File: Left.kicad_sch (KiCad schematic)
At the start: 30 parts, among them J5 Conn_01x02, U1 LM1117-3.3, U10 RP2040, U8 W25Q128JVS, Y2 ECS-120-8-33-JGN-TR3

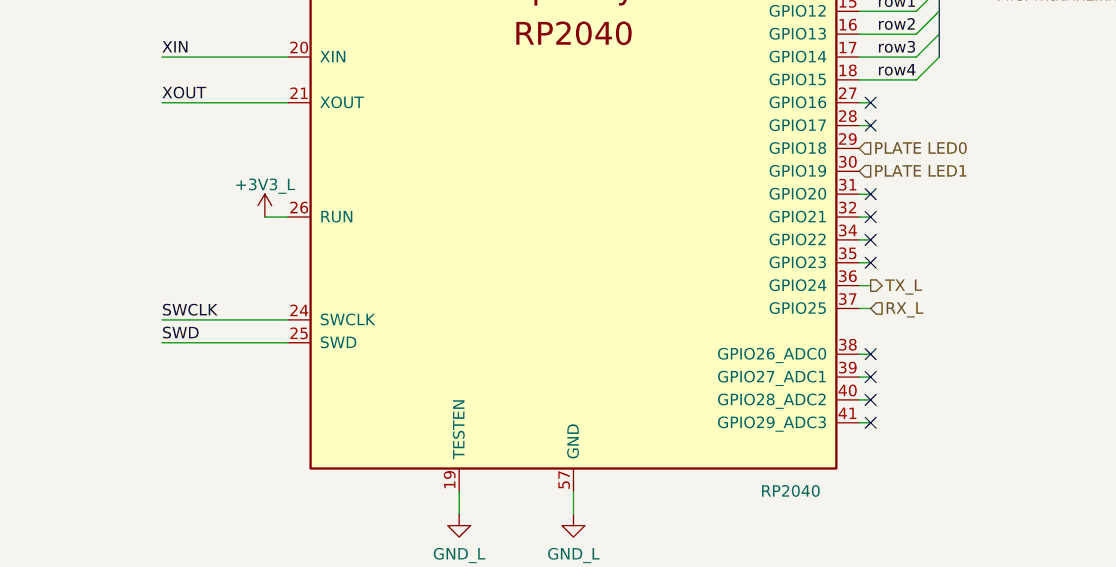
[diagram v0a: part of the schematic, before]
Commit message: Left side case created in blender
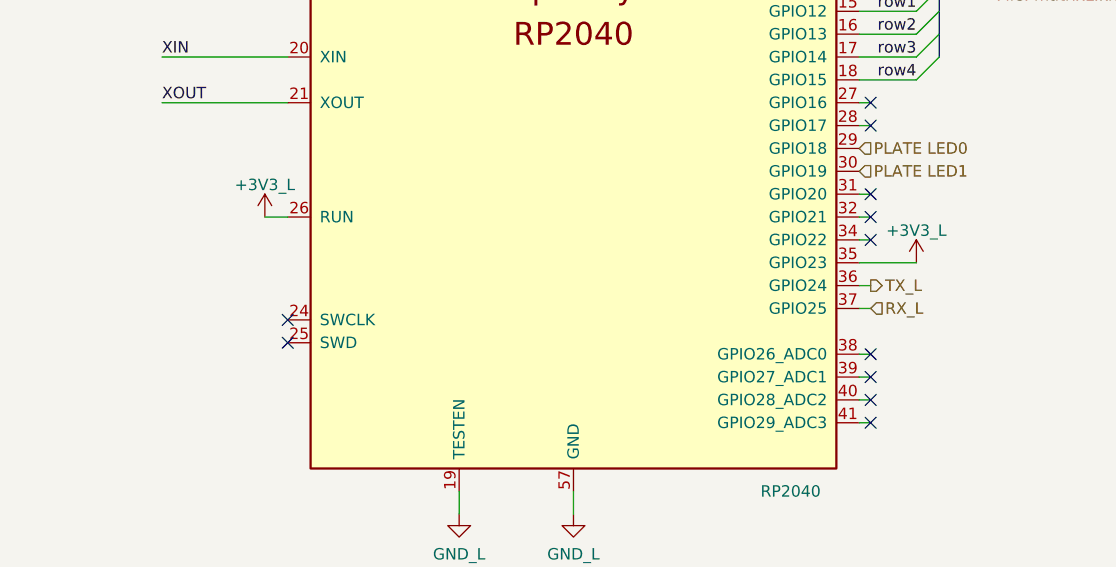
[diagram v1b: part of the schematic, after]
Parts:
- H1, H3, H4: footprint MountingHole:MountingHole_3.2mm_M3_Pad_Via -> arisu-split:aluminium profile nut
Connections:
- net +3V3_L: now also U10.35 (GPIO23)
- net SWCLK: no longer names the net of U10.24 (SWCLK)
- net SWD: no longer names the net of U10.25 (SWD)
- no-connect marks 14 -> 15
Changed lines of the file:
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@@
   (no_connect (at 200.66 78.74))
   (no_connect (at 201.93 149.86))
-  (no_connect (at 201.93 137.16))
+  (no_connect (at 137.16 143.51))
   (no_connect (at 201.93 129.54))
   (no_connect (at 200.66 83.82))
@@
   (no_connect (at 200.66 81.28))
   (no_connect (at 201.93 152.4))
+  (no_connect (at 137.16 146.05))
   (bus_entry (at 209.55 88.9) (size -2.54 2.54)
     (stroke (width 0) (type default) (color 0 0 0 0))
@@
     (stroke (width 0) (type default) (color 0 0 0 0))
   )
-  (wire (pts (xy 137.16 146.05) (xy 123.19 146.05))
-    (stroke (width 0) (type default) (color 0 0 0 0))
-  )
   (wire (pts (xy 123.19 91.44) (xy 137.16 91.44))
     (stroke (width 0) (type default) (color 0 0 0 0))
@@
     (stroke (width 0) (type default) (color 0 0 0 0))
   )
-  (wire (pts (xy 137.16 143.51) (xy 123.19 143.51))
-    (stroke (width 0) (type default) (color 0 0 0 0))
-  )
   (wire (pts (xy 45.72 163.83) (xy 59.69 163.83))
     (stroke (width 0) (type default) (color 0 0 0 0))
@@
     (stroke (width 0) (type default) (color 0 0 0 0))
   )
-  (wire (pts (xy 201.93 137.16) (xy 200.66 137.16))
+  (wire (pts (xy 200.66 137.16) (xy 207.01 137.16))
     (stroke (width 0) (type default) (color 0 0 0 0))
   )
@@
     (effects (font (size 1.27 1.27)) (justify right bottom))
   )
-  (label "SWD" (at 123.19 146.05 0)
-    (effects (font (size 1.27 1.27)) (justify left bottom))
-  )
   (label "1V1" (at 148.59 27.94 180)
     (effects (font (size 1.27 1.27)) (justify right bottom))
@@
     (effects (font (size 1.27 1.27)) (justify right bottom))
   )
-  (label "SWCLK" (at 123.19 143.51 0)
-    (effects (font (size 1.27 1.27)) (justify left bottom))
-  )
   (label "col3" (at 207.01 93.98 180)
     (effects (font (size 1.27 1.27)) (justify right bottom))
@@
       (effects (font (size 1.27 1.27)) (justify left))
     )
-    (property "Footprint" "MountingHole:MountingHole_3.2mm_M3_Pad_Via" (id 2) (at 154.94 187.96 0)
+    (property "Footprint" "arisu-split:aluminium profile nut" (id 2) (at 154.94 187.96 0)
       (effects (font (size 1.27 1.27)) hide)
     )
@@
       (effects (font (size 1.27 1.27)) (justify left))
     )
-    (property "Footprint" "MountingHole:MountingHole_3.2mm_M3_Pad_Via" (id 2) (at 132.08 187.96 0)
+    (property "Footprint" "arisu-split:aluminium profile nut" (id 2) (at 132.08 187.96 0)
       (effects (font (size 1.27 1.27)) hide)
     )
@@
       (effects (font (size 1.27 1.27)) (justify left))
     )
-    (property "Footprint" "MountingHole:MountingHole_3.2mm_M3_Pad_Via" (id 2) (at 132.08 175.26 0)
+    (property "Footprint" "arisu-split:aluminium profile nut" (id 2) (at 132.08 175.26 0)
       (effects (font (size 1.27 1.27)) hide)
     )
@@
     (pin "2")
   )
+  (symbol (lib_id "arisu-split:+3V3_L") (at 207.01 137.16 0) (unit 1)
+    (in_bom yes) (on_board yes) (fields_autoplaced)
+    (property "Reference" "#PWR0165" (id 0) (at 207.01 140.97 0)
+      (effects (font (size 1.27 1.27)) hide)
+    )
+    (property "Value" "+3V3_L" (id 1) (at 207.01 133.5842 0))
+    (property "Footprint" "" (id 2) (at 207.01 137.16 0)
+      (effects (font (size 1.27 1.27)) hide)
+    )
+    (property "Datasheet" "" (id 3) (at 207.01 137.16 0)
+      (effects (font (size 1.27 1.27)) hide)
+    )
+    (pin "1")
+  )
   (symbol (lib_id "Device:R") (at 215.9 63.5 270) (unit 1)

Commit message: replace usb right side, rotate micro, add protection diodes, trrs protection circuit mirrored, run pin cap removved, resistor footprints replaced
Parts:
- R13, R14, R16, R17: footprint Capacitor_SMD:C_0603_1608Metric -> Resistor_SMD:R_0603_1608Metric
- R15: footprint Capacitor_SMD:C_0402_1005Metric -> Resistor_SMD:R_0402_1005Metric
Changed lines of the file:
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@@
     (property "Reference" "R15" (id 0) (at 63.5 158.5722 90))
     (property "Value" "1k" (id 1) (at 63.5 160.8836 90))
-    (property "Footprint" "Capacitor_SMD:C_0402_1005Metric" (id 2) (at 63.5 162.052 90)
+    (property "Footprint" "Resistor_SMD:R_0402_1005Metric" (id 2) (at 63.5 162.052 90)
       (effects (font (size 1.27 1.27)) hide)
     )
@@
     (property "Reference" "R17" (id 0) (at 215.9 65.8622 90))
     (property "Value" "27" (id 1) (at 215.9 68.1736 90))
-    (property "Footprint" "Capacitor_SMD:C_0603_1608Metric" (id 2) (at 215.9 69.342 90)
+    (property "Footprint" "Resistor_SMD:R_0603_1608Metric" (id 2) (at 215.9 69.342 90)
       (effects (font (size 1.27 1.27)) hide)
     )
@@
       (effects (font (size 1.27 1.27)) (justify left))
     )
-    (property "Footprint" "Capacitor_SMD:C_0603_1608Metric" (id 2) (at 56.642 86.36 90)
+    (property "Footprint" "Resistor_SMD:R_0603_1608Metric" (id 2) (at 56.642 86.36 90)
       (effects (font (size 1.27 1.27)) hide)
     )
@@
     (property "Reference" "R13" (id 0) (at 43.18 96.3422 90))
     (property "Value" "1k" (id 1) (at 43.18 98.6536 90))
-    (property "Footprint" "Capacitor_SMD:C_0603_1608Metric" (id 2) (at 43.18 99.822 90)
+    (property "Footprint" "Resistor_SMD:R_0603_1608Metric" (id 2) (at 43.18 99.822 90)
       (effects (font (size 1.27 1.27)) hide)
     )
@@
     (property "Reference" "R16" (id 0) (at 215.9 58.2422 90))
     (property "Value" "27" (id 1) (at 215.9 60.5536 90))
-    (property "Footprint" "Capacitor_SMD:C_0603_1608Metric" (id 2) (at 215.9 61.722 90)
-      (effects (font (size 1.27 1.27)) hide)
-    )
+    (property "Footprint" "Resistor_SMD:R_0603_1608Metric" (id 2) (at 215.9 61.722 90)
+      (effects (font (size 1.27 1.27)) hide)
+    )

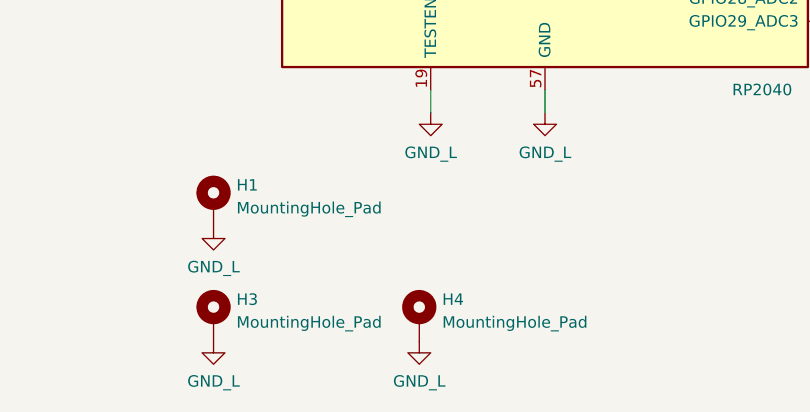
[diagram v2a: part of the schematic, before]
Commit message: Add back logo, improve layers for 3d model, remove silkscreen designators, basically fix right pcb
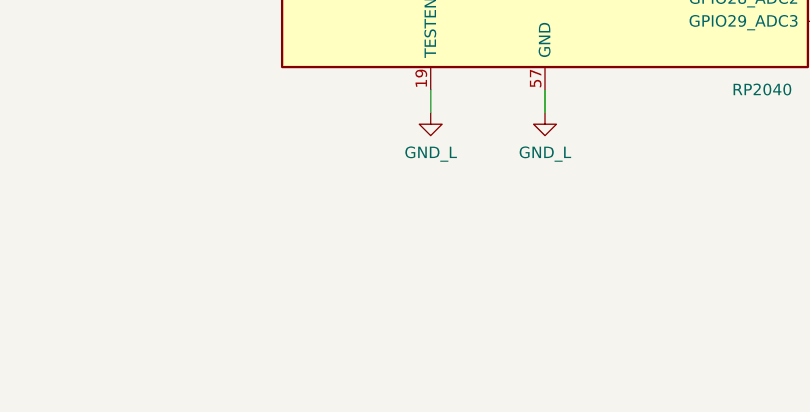
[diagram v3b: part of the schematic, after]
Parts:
- removed H1, H3, H4: MountingHole_Pad, arisu-split:aluminium profile nut, symbol Mechanical:MountingHole_Pad
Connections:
- net PLATE  LED1 renamed PLATE LED1
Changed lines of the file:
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@@
     (effects (font (size 1.27 1.27)) (justify left))
   )
-  (hierarchical_label "PLATE  LED1" (shape input) (at 200.66 127 0)
+  (hierarchical_label "PLATE LED1" (shape input) (at 200.66 127 0)
     (effects (font (size 1.27 1.27)) (justify left))
   )
@@
     (pin "1")
     (pin "2")
-  )
-  (symbol (lib_id "Mechanical:MountingHole_Pad") (at 154.94 187.96 0) (unit 1)
-    (in_bom yes) (on_board yes) (fields_autoplaced)
-    (property "Reference" "H4" (id 0) (at 157.48 185.8553 0)
-      (effects (font (size 1.27 1.27)) (justify left))
-    )
-    (property "Value" "MountingHole_Pad" (id 1) (at 157.48 188.3922 0)
-      (effects (font (size 1.27 1.27)) (justify left))
-    )
-    (property "Footprint" "arisu-split:aluminium profile nut" (id 2) (at 154.94 187.96 0)
-      (effects (font (size 1.27 1.27)) hide)
-    )
-    (property "Datasheet" "~" (id 3) (at 154.94 187.96 0)
-      (effects (font (size 1.27 1.27)) hide)
-    )
-    (pin "1")
   )
   (symbol (lib_id "Device:R") (at 63.5 163.83 270) (unit 1)
@@
     (pin "2")
   )
-  (symbol (lib_id "arisu-split:GND_L") (at 132.08 177.8 0) (unit 1)
-    (in_bom yes) (on_board yes) (fields_autoplaced)
-    (property "Reference" "#PWR0153" (id 0) (at 132.08 184.15 0)
-      (effects (font (size 1.27 1.27)) hide)
-    )
-    (property "Value" "GND_L" (id 1) (at 132.08 182.2434 0))
-    (property "Footprint" "" (id 2) (at 132.08 177.8 0)
-      (effects (font (size 1.27 1.27)) hide)
-    )
-    (property "Datasheet" "" (id 3) (at 132.08 177.8 0)
-      (effects (font (size 1.27 1.27)) hide)
-    )
-    (pin "1")
-  )
   (symbol (lib_id "arisu-split:GND_L") (at 128.27 39.37 0) (unit 1)
     (in_bom yes) (on_board yes) (fields_autoplaced)
@@
     (pin "1")
     (pin "2")
-  )
-  (symbol (lib_id "arisu-split:GND_L") (at 154.94 190.5 0) (unit 1)
-    (in_bom yes) (on_board yes) (fields_autoplaced)
-    (property "Reference" "#PWR0108" (id 0) (at 154.94 196.85 0)
-      (effects (font (size 1.27 1.27)) hide)
-    )
-    (property "Value" "GND_L" (id 1) (at 154.94 194.9434 0))
-    (property "Footprint" "" (id 2) (at 154.94 190.5 0)
-      (effects (font (size 1.27 1.27)) hide)
-    )
-    (property "Datasheet" "" (id 3) (at 154.94 190.5 0)
-      (effects (font (size 1.27 1.27)) hide)
-    )
-    (pin "1")
-  )
-  (symbol (lib_id "Mechanical:MountingHole_Pad") (at 132.08 187.96 0) (unit 1)
-    (in_bom yes) (on_board yes)
-    (property "Reference" "H3" (id 0) (at 134.62 185.8553 0)
-      (effects (font (size 1.27 1.27)) (justify left))
-    )
-    (property "Value" "MountingHole_Pad" (id 1) (at 134.62 188.3922 0)
-      (effects (font (size 1.27 1.27)) (justify left))
-    )
-    (property "Footprint" "arisu-split:aluminium profile nut" (id 2) (at 132.08 187.96 0)
-      (effects (font (size 1.27 1.27)) hide)
-    )
-    (property "Datasheet" "~" (id 3) (at 132.08 187.96 0)
-      (effects (font (size 1.27 1.27)) hide)
-    )
-    (pin "1")
   )
   (symbol (lib_id "Device:C") (at 80.01 82.55 0) (unit 1)
@@
     (pin "4")
   )
-  (symbol (lib_id "Mechanical:MountingHole_Pad") (at 132.08 175.26 0) (unit 1)
-    (in_bom yes) (on_board yes) (fields_autoplaced)
-    (property "Reference" "H1" (id 0) (at 134.62 173.1553 0)
-      (effects (font (size 1.27 1.27)) (justify left))
-    )
-    (property "Value" "MountingHole_Pad" (id 1) (at 134.62 175.6922 0)
-      (effects (font (size 1.27 1.27)) (justify left))
-    )
-    (property "Footprint" "arisu-split:aluminium profile nut" (id 2) (at 132.08 175.26 0)
-      (effects (font (size 1.27 1.27)) hide)
-    )
-    (property "Datasheet" "~" (id 3) (at 132.08 175.26 0)
-      (effects (font (size 1.27 1.27)) hide)
-    )
-    (pin "1")
-  )
   (symbol (lib_id "arisu-split:GND_L") (at 85.09 87.63 0) (unit 1)
     (in_bom yes) (on_board yes) (fields_autoplaced)
@@
       (effects (font (size 1.27 1.27)) hide)
     )
-    (pin "1")
-  )
-  (symbol (lib_id "arisu-split:GND_L") (at 132.08 190.5 0) (unit 1)
-    (in_bom yes) (on_board yes) (fields_autoplaced)
-    (property "Reference" "#PWR0151" (id 0) (at 132.08 196.85 0)
-      (effects (font (size 1.27 1.27)) hide)
-    )
-    (property "Value" "GND_L" (id 1) (at 132.08 194.9434 0))
-    (property "Footprint" "" (id 2) (at 132.08 190.5 0)
-      (effects (font (size 1.27 1.27)) hide)
-    )
-    (property "Datasheet" "" (id 3) (at 132.08 190.5 0)
-      (effects (font (size 1.27 1.27)) hide)
-    )
